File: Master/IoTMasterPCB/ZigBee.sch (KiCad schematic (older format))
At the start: 0 parts

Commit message: Added some components for Master Board schematic.
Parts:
- added U?: AT86RF232-ZX, Personal_ICs:AT86RF232-ZX, symbol Personal_ICs:AT86RF232-ZX
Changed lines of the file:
@@
 $Descr A4 11693 8268
 encoding utf-8
-Sheet 1 6
+Sheet 5 6
 Title "IoT Master Board"
 Date "2020-11-28"
@@
 Comment4 ""
 $EndDescr
+$Comp
+L Personal_ICs:AT86RF232-ZX U?
+U 1 1 5FCB565A
+P 4650 2800
+F 0 "U?" H 5550 3187 60  0000 C CNN
+F 1 "AT86RF232-ZX" H 5550 3081 60  0000 C CNN
+F 2 "Personal_ICs:AT86RF232-ZX" H 5550 3040 60  0001 C CNN
+F 3 "" H 4650 2800 60  0000 C CNN
+	1    4650 2800
+	1    0    0    -1
+$EndComp
 $EndSCHEMATC

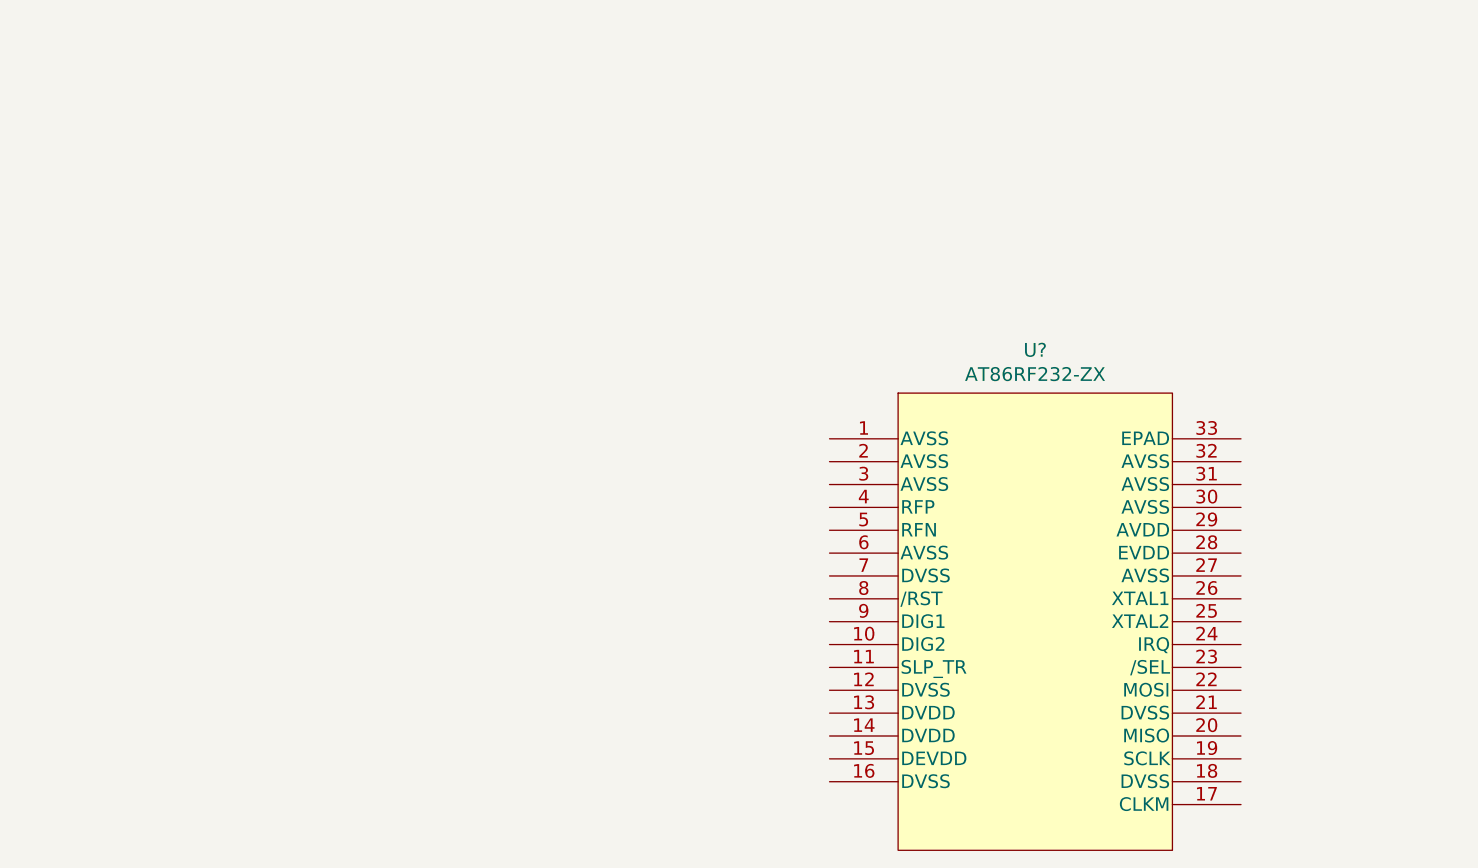
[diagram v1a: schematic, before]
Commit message: Work on Master Board schematics; added full Zigbee. Added RFID module. Added USB/power supply, as well as MCU decoupling.
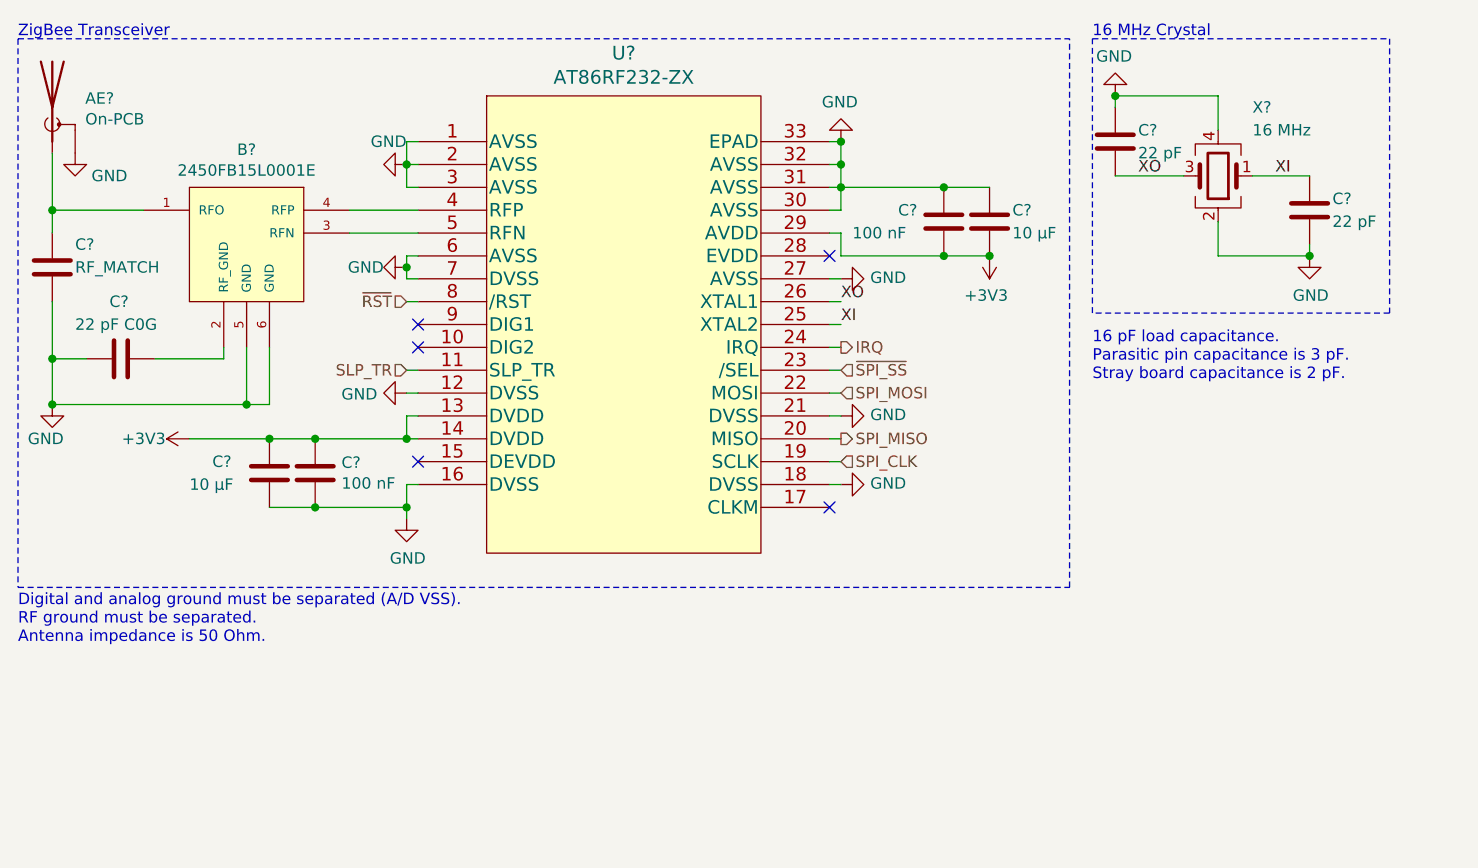
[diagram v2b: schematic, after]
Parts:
- removed U?: AT86RF232-ZX, Personal_ICs:AT86RF232-ZX, symbol Personal_ICs:AT86RF232-ZX
- added AE?: On-PCB, RF_Antenna:Texas_SWRA117D_2.4GHz_Left, symbol Device:Antenna_Shield
- added B?: 2450FB15L0001E, Personal_Passives:2450FB15L0001E, symbol Personal_Passives:2450FB15L0001E
- added C? (x2): 100 nF, Capacitor_SMD:C_0603_1608Metric, symbol Device:C
- added C? (x2): 22 pF, Capacitor_SMD:C_0603_1608Metric, symbol Device:C
- added C?: 22 pF C0G, Capacitor_SMD:C_0402_1005Metric, symbol Device:C
- added C?: RF_MATCH, Capacitor_SMD:C_0805_2012Metric, symbol Device:C
- added C? (x2): 10 µF, Capacitor_SMD:C_0805_2012Metric, symbol Device:C
- added U?: AT86RF232-ZX, Personal_ICs:AT86RF232-ZX, symbol Personal_ICs:AT86RF232-ZX
- added X?: 16 MHz, Personal_Actives:ECS1601633BCKMTR, symbol Device:Crystal_GND24
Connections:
- new net: B?.4 (RFP), U?.4 (RFP)
- new net: B?.3 (RFN), U?.5 (RFN)
- new net: AE?.1 (A), B?.1 (RFO), C?.1
- new net: B?.2 (RF_GND), C?.1
- new net +3V3: C?.1, C?.1, C?.2, C?.2, U?.13 (DVDD), U?.14 (DVDD), U?.29 (AVDD)
- new net GND: AE?.2 (Shield), B?.5 (GND), B?.6 (GND), C?.1, C?.1, C?.1, C?.2, C?.2, C?.2, C?.2, C?.2, U?.1 (AVSS), U?.12 (DVSS), U?.16 (DVSS), U?.18 (DVSS), U?.2 (AVSS), U?.21 (DVSS), U?.27 (AVSS), U?.3 (AVSS), U?.30 (AVSS), U?.31 (AVSS), U?.32 (AVSS), U?.33 (EPAD), U?.6 (AVSS), U?.7 (DVSS), X?.2, X?.4
- new net IRQ: U?.24 (IRQ)
- new net SLP_TR: U?.11 (SLP_TR)
- new net SPI_CLK: U?.19 (SCLK)
- new net SPI_MISO: U?.20 (MISO)
- new net SPI_MOSI: U?.22 (MOSI)
- new net XI: C?.1, U?.25 (XTAL2), X?.1
- new net XO: C?.2, U?.26 (XTAL1), X?.3
- new net ~RST: U?.8 (/RST)
- new net ~SPI_SS: U?.23 (/SEL)
- no-connect marks 0 -> 5
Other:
- note added: "16 MHz Crystal"
- note added: "16 pF load capacitance.\nParasitic pin capacitance is 3 pF.\nStray board capacitance is 2 pF."
- note added: "Digital and analog ground must be separated (A/D VSS).\nRF ground must be separated.\nAntenna impedance is 50 Ohm."
- note added: "ZigBee Transceiver"

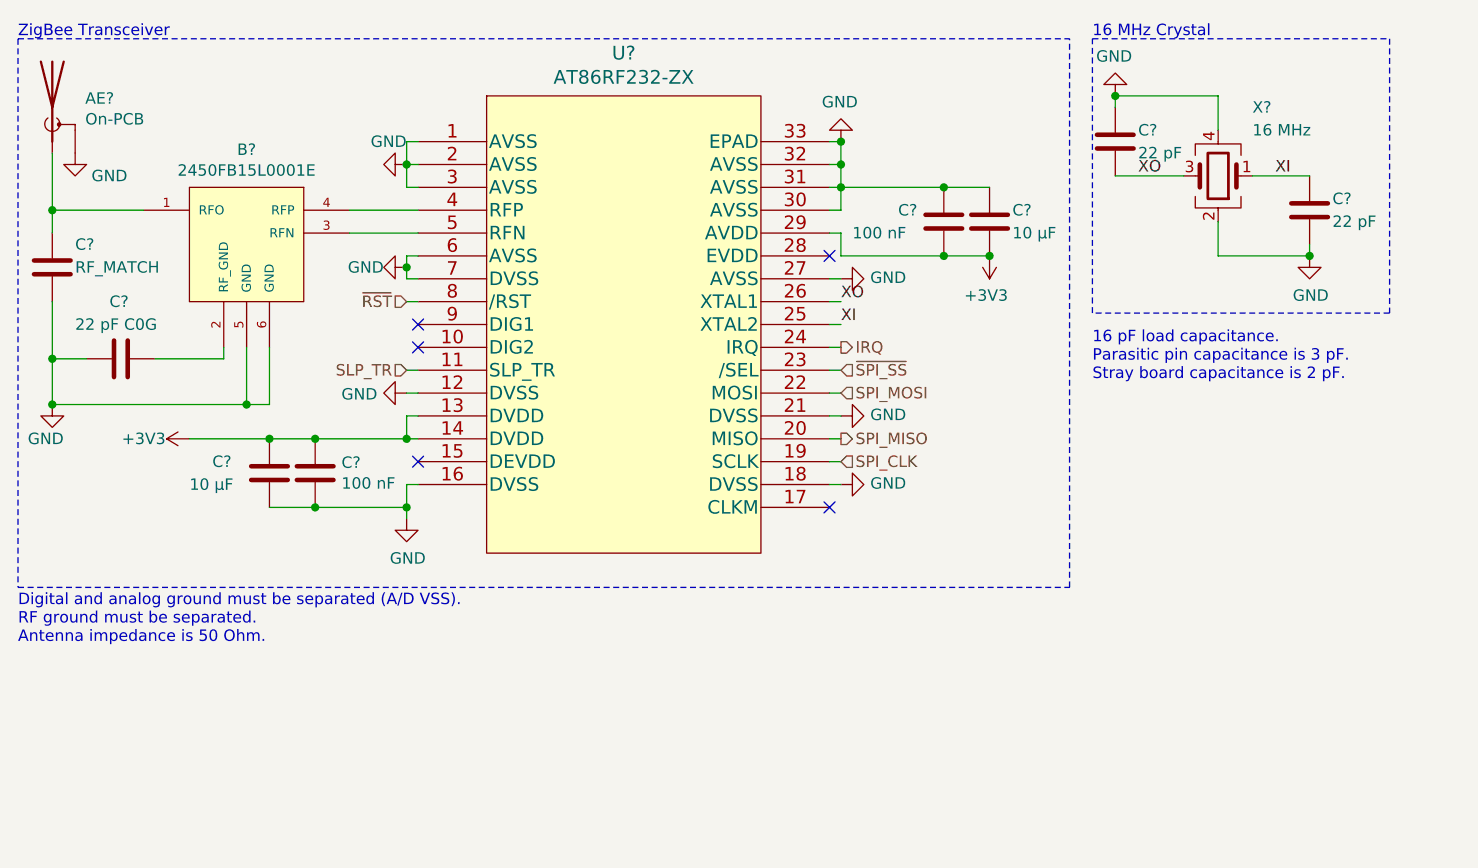
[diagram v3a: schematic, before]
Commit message: Finished RFID module sans antenna footprint. Added KSZ8081MNX and hierarchial connections.
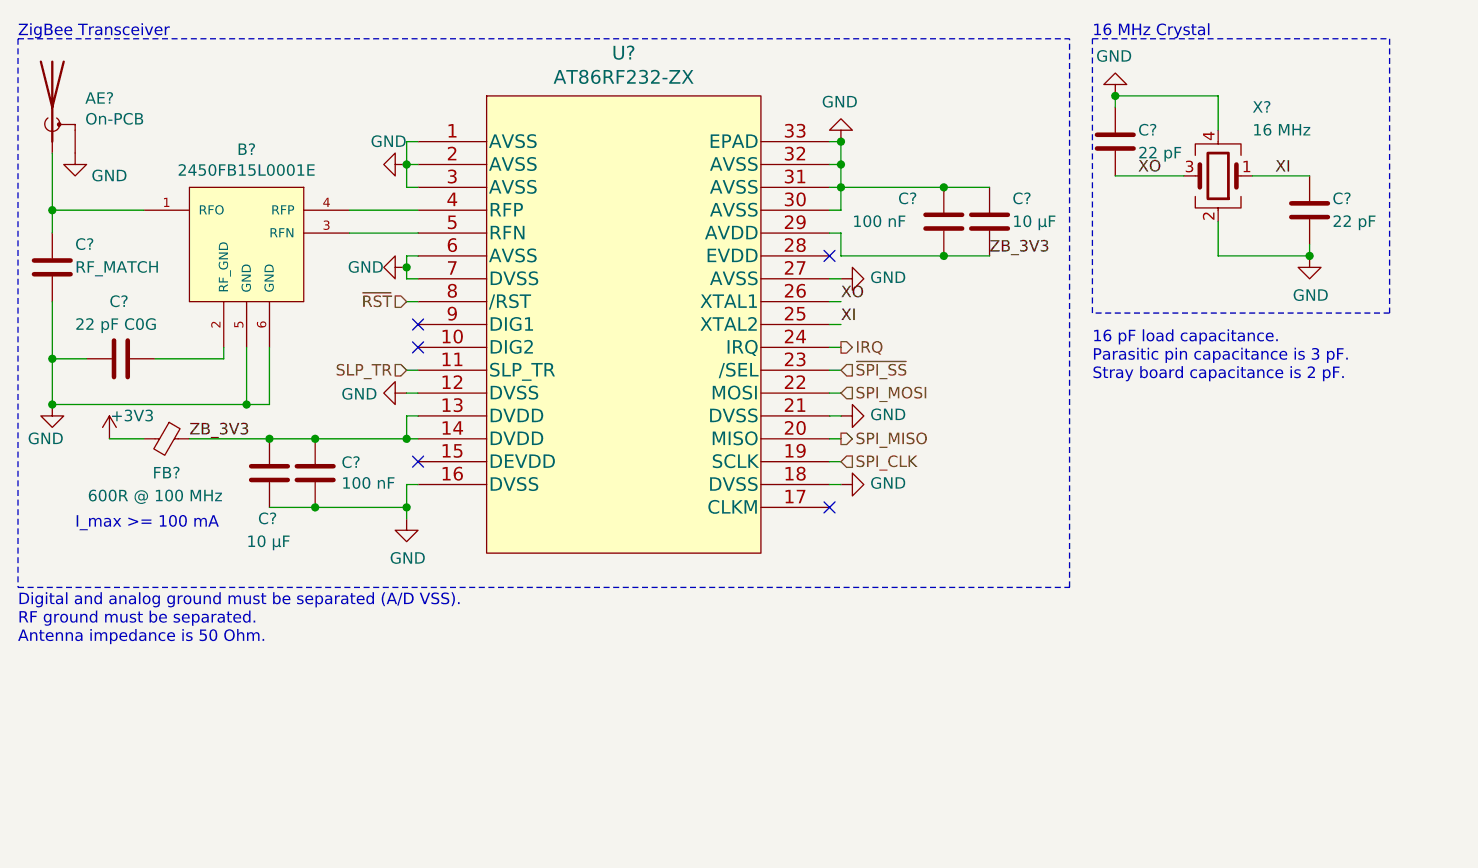
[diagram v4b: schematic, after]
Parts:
- added FB?: 600R @ 100 MHz, symbol Device:Ferrite_Bead_Small
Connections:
- net +3V3: now also FB?.2; no longer C?.1, C?.1, C?.2, C?.2, U?.13 (DVDD), U?.14 (DVDD), U?.29 (AVDD)
- new net ZB_3V3: C?.1, C?.1, C?.2, C?.2, FB?.1, U?.13 (DVDD), U?.14 (DVDD), U?.29 (AVDD)
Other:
- note added: "I_max >= 100 mA"
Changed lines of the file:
@@
 U 1 1 5FCC57EF
 P 5150 1850
-F 0 "C?" H 4950 1900 50  0000 L CNN
-F 1 "100 nF" H 4750 1800 50  0000 L CNN
+F 0 "C?" H 4950 1950 50  0000 L CNN
+F 1 "100 nF" H 4750 1850 50  0000 L CNN
 F 2 "Capacitor_SMD:C_0603_1608Metric" H 5188 1700 50  0001 C CNN
 F 3 "~" H 5150 1850 50  0001 C CNN
@@
 U 1 1 5FCC588D
 P 5350 1850
-F 0 "C?" H 5450 1900 50  0000 L CNN
-F 1 "10 µF" H 5450 1800 50  0000 L CNN
+F 0 "C?" H 5450 1950 50  0000 L CNN
+F 1 "10 µF" H 5450 1850 50  0000 L CNN
 F 2 "Capacitor_SMD:C_0805_2012Metric" H 5388 1700 50  0001 C CNN
 F 3 "~" H 5350 1850 50  0001 C CNN
@@
 U 1 1 5FCC5899
 P 2200 2950
-F 0 "C?" H 1950 3000 50  0000 L CNN
-F 1 "10 µF" H 1850 2900 50  0000 L CNN
+F 0 "C?" H 2150 2750 50  0000 L CNN
+F 1 "10 µF" H 2100 2650 50  0000 L CNN
 F 2 "Capacitor_SMD:C_0805_2012Metric" H 2238 2800 50  0001 C CNN
 F 3 "~" H 2200 2950 50  0001 C CNN
@@
 $Comp
 L power:+3V3 #PWR?
-U 1 1 5FCC844A
-P 5350 2000
-F 0 "#PWR?" H 5350 1850 50  0001 C CNN
-F 1 "+3V3" H 5365 2173 50  0000 C CNN
-F 2 "" H 5350 2000 50  0001 C CNN
-F 3 "" H 5350 2000 50  0001 C CNN
-	1    5350 2000
-	-1   0    0    1
-$EndComp
-Connection ~ 5350 2000
-$Comp
-L power:+3V3 #PWR?
 U 1 1 5FCC9953
-P 1850 2800
-F 0 "#PWR?" H 1850 2650 50  0001 C CNN
-F 1 "+3V3" V 1850 3000 50  0000 C CNN
-F 2 "" H 1850 2800 50  0001 C CNN
-F 3 "" H 1850 2800 50  0001 C CNN
-	1    1850 2800
-	0    -1   -1   0
-$EndComp
+P 1500 2800
+F 0 "#PWR?" H 1500 2650 50  0001 C CNN
+F 1 "+3V3" H 1600 2900 50  0000 C CNN
+F 2 "" H 1500 2800 50  0001 C CNN
+F 3 "" H 1500 2800 50  0001 C CNN
+	1    1500 2800
+	1    0    0    -1
+$EndComp
+$Comp
+L Device:Ferrite_Bead_Small FB?
+U 1 1 5FE2F067
+P 1750 2800
+F 0 "FB?" V 1900 2800 50  0000 C CNN
+F 1 "600R @ 100 MHz" V 2000 2750 50  0000 C CNN
+F 2 "" V 1680 2800 50  0001 C CNN
+F 3 "~" H 1750 2800 50  0001 C CNN
+	1    1750 2800
+	0    1    1    0
+$EndComp
+Wire Wire Line
+	1500 2800 1650 2800
+Text Label 1850 2800 0    50   ~ 0
+ZB_3V3
+Text Label 5350 2000 0    50   ~ 0
+ZB_3V3
+Text Notes 1350 3200 0    50   ~ 0
+I_max >= 100 mA
 $EndSCHEMATC
